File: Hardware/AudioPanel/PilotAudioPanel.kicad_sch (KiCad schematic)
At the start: 0 parts

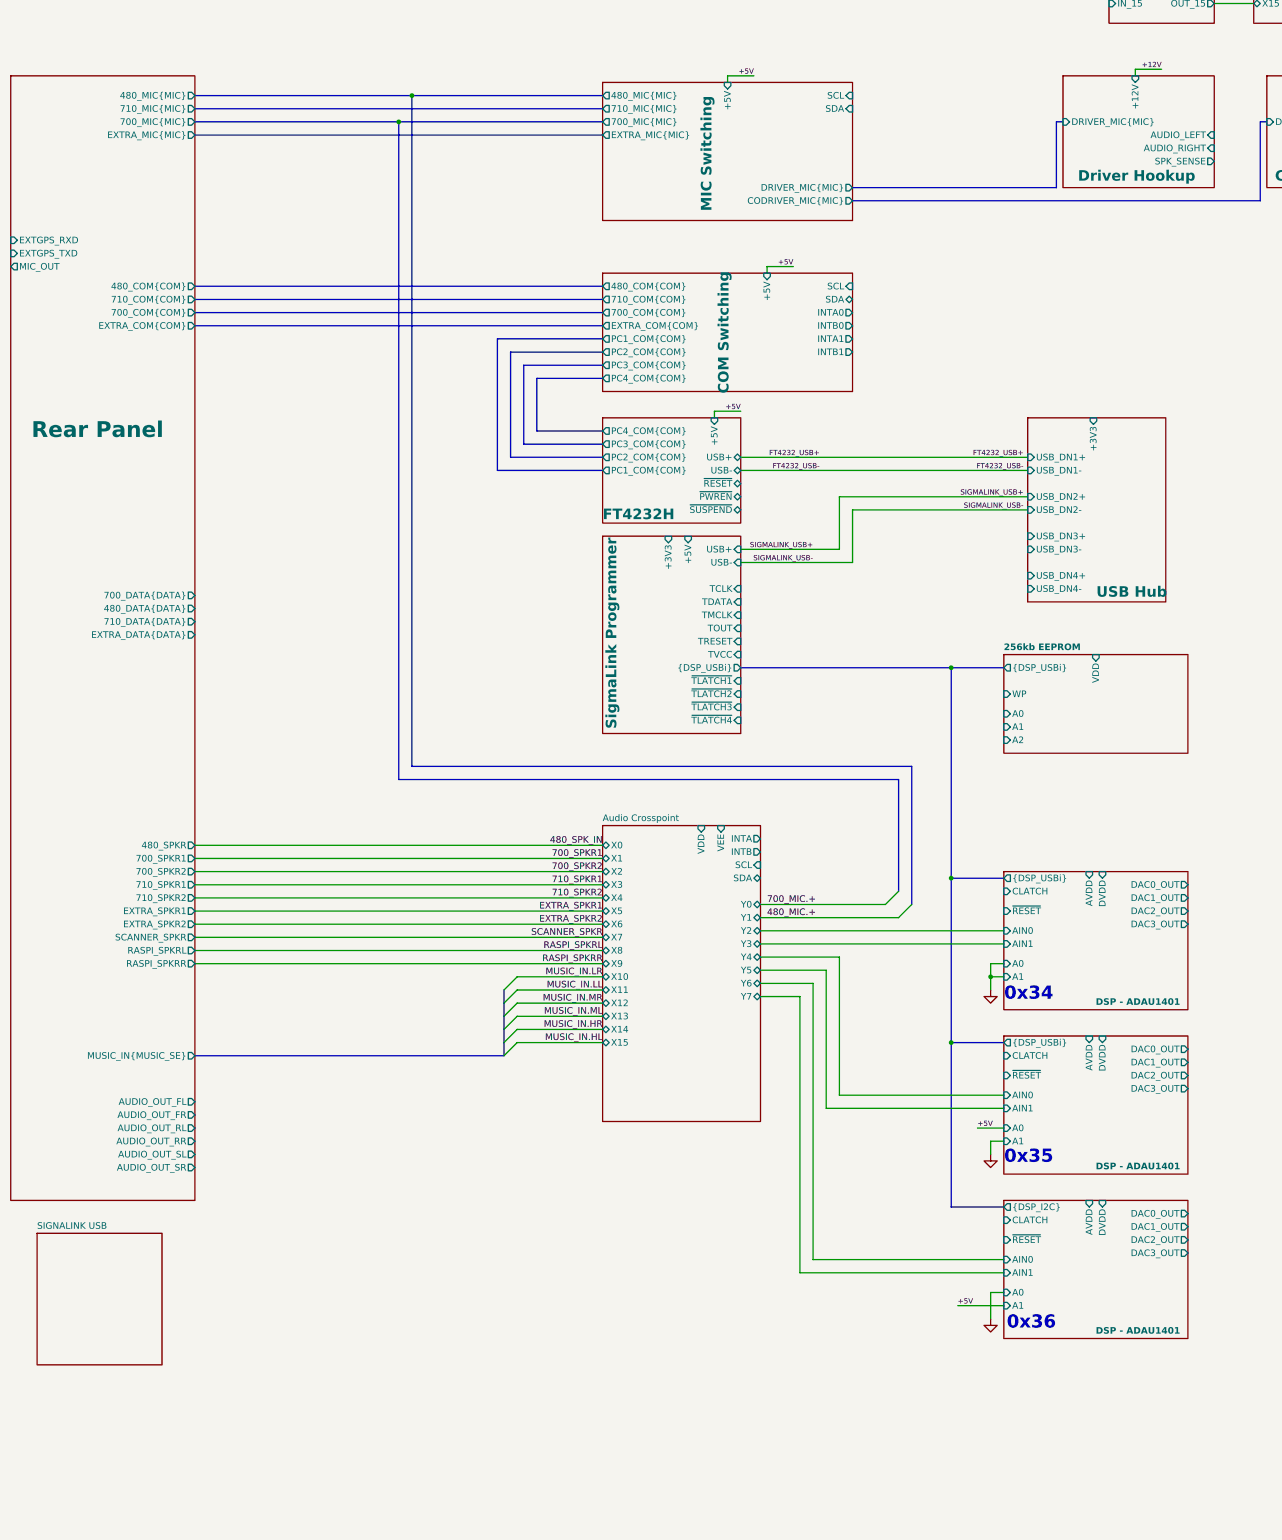
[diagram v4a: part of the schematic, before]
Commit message: Added DATA switching to COM switching page
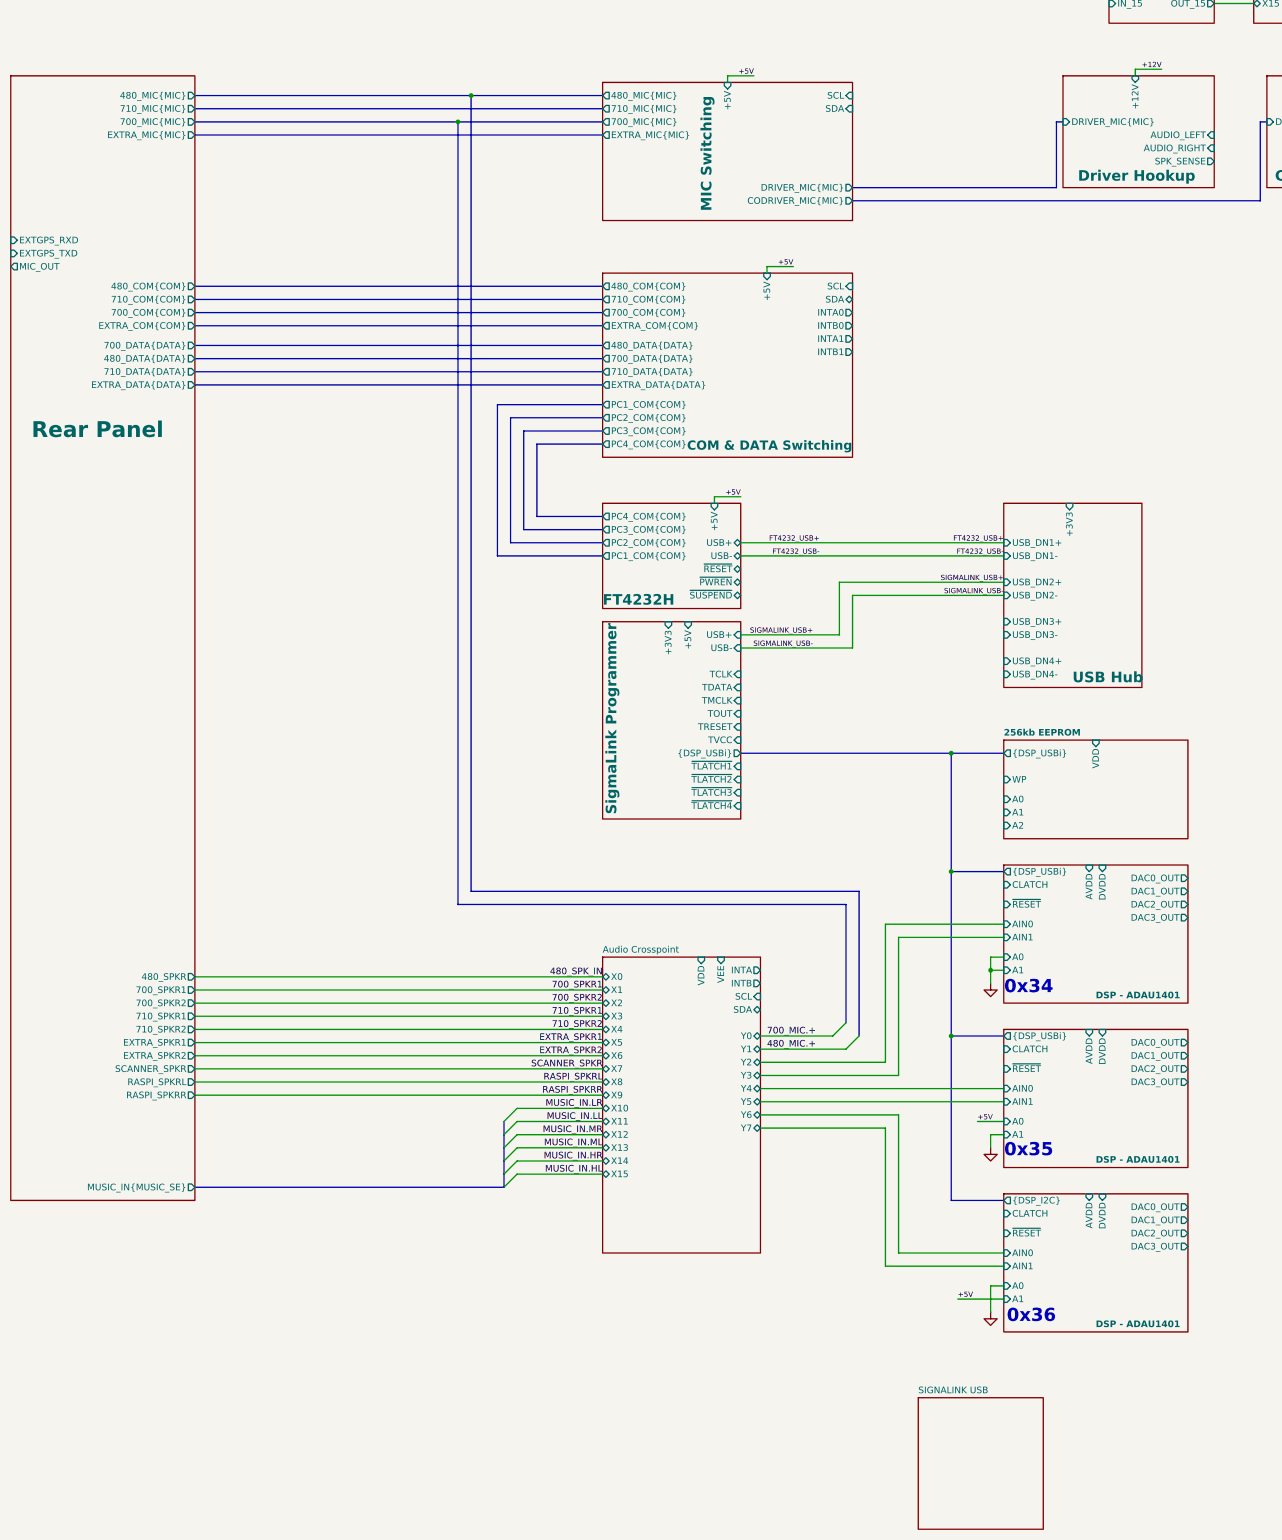
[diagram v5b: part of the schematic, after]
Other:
- sheet COM Switching renamed COM & DATA Switching
- sheet COM & DATA Switching: file MUX_COM_74LVC4066.kicad_sch -> COM_DATA_Switching.kicad_sch
- sheet COM & DATA Switching ports: added 480_DATA{DATA}, 700_DATA{DATA}, 710_DATA{DATA}, EXTRA_DATA{DATA}; removed none
- sheet Rear Panel ports: added none; removed AUDIO_OUT_FL, AUDIO_OUT_FR, AUDIO_OUT_RL, AUDIO_OUT_RR, AUDIO_OUT_SL, AUDIO_OUT_SR

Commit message: Cleaned up stuff, defined more busses
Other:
- sheet 256kb EEPROM renamed 256kb DSP EEPROM
- added sheet +12V Regulator (PSU_12V_R-78.kicad_sch)
- added sheet +5V Regulator (PSU_5V_R-78.kicad_sch)
- added sheet -12V Regulator (PSU_-12V_TL497.kicad_sch)
- sheet DSP - ADAU1401 ports: added {DSP_USBi}; removed {DSP_I2C}
- sheet FT4232H ports: added FT4232H{USB}; removed USB+, USB-
- sheet MIC Switching ports: added CROSSMIC_A, CROSSMIC_B; removed none
- sheet Rear Panel ports: added AUDIO_OUT_FL, AUDIO_OUT_FR, AUDIO_OUT_RL, AUDIO_OUT_RR, AUDIO_OUT_SL, AUDIO_OUT_SR, USB_HOST{USB}, VIN_PROTECTED; removed none
- sheet SIGNALINK USB ports: added RIGCTRL_SIGNALINK{USB}; removed none
- sheet SigmaLink Programmer ports: added DSP_SIGMALINK{USB}, ~{TLATCH5}; removed USB+, USB-
- sheet USB Hub ports: added DSP_SIGMALINK{USB}, FT4232H{USB}, RIGCTRL_SIGNALINK{USB}, USB_HOST{USB}; removed USB_DN1+, USB_DN1-, USB_DN2+, USB_DN2-, USB_DN3+, USB_DN3-, USB_DN4+, USB_DN4-

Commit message: Removed extraneous pages
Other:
- removed sheet Crosspoint Switch - COM Port Switching
- removed sheet Crosspoint Switch - DATA Port Switching
- removed sheet Crosspoint Switch - MIC Port Switching
- removed sheet Crosspoint Switch - MT8816
- removed sheet DSP - ADAV400
- removed sheet Input Buffer
- removed sheet Output Buffer

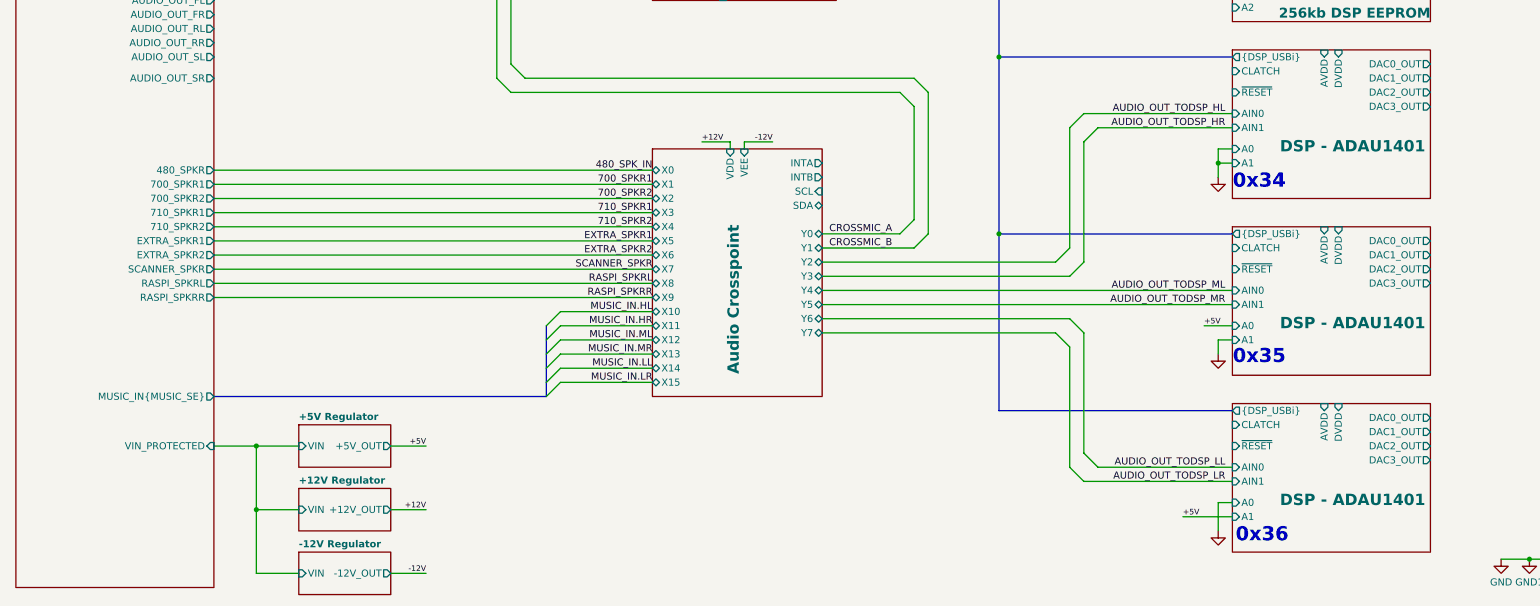
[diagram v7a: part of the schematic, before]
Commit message: Laid groundwork for stereo DSP routing
I figured it out. I need to combine the left audio channels, combine the right audio channels, pass both to the DSP chips. Each audio zone will eventually have its own DSP to handle crossovers and time delay and things.

Use the Pioneer Network Mode for easier frequency separation.

To do: add active summing amplifers to combine left and right sub-channels
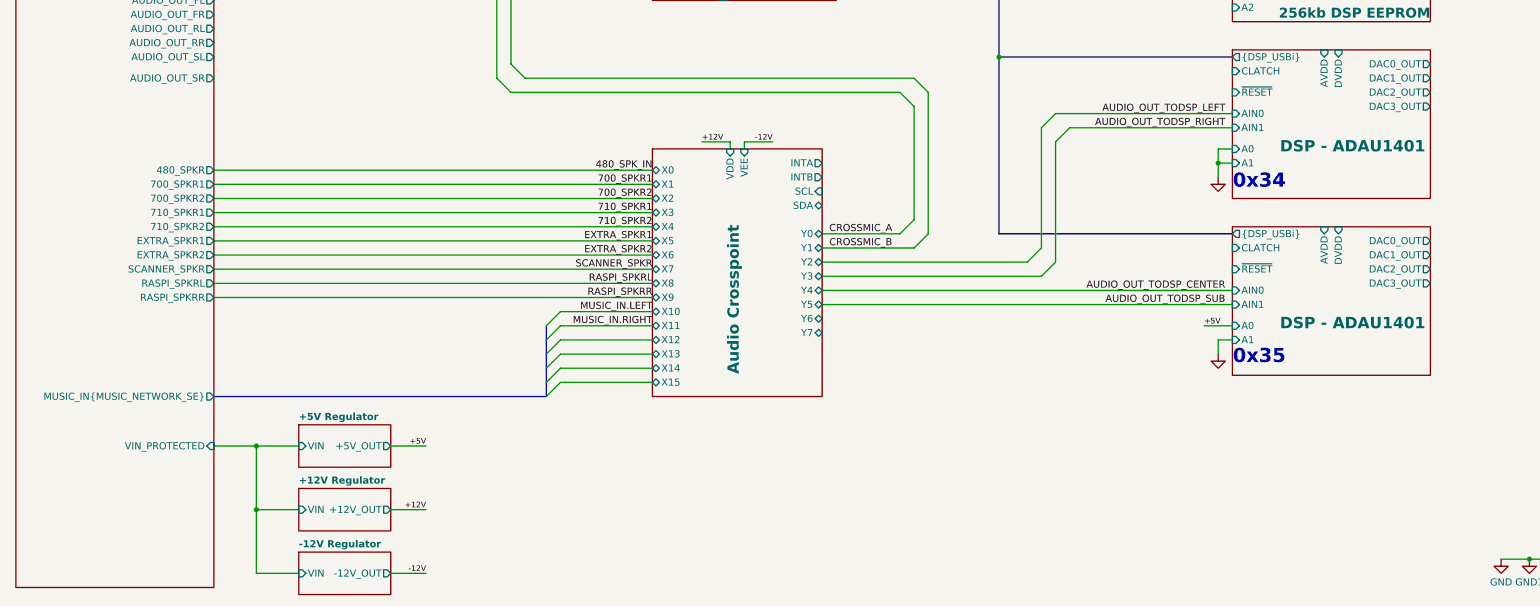
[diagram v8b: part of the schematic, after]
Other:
- sheet Rear Panel ports: added MUSIC_IN{MUSIC_NETWORK_SE}; removed MUSIC_IN{MUSIC_SE}
- note removed: "0x36"
